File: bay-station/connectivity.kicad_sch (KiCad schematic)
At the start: 4 parts, among them U3 ESP32-S3-WROOM-1

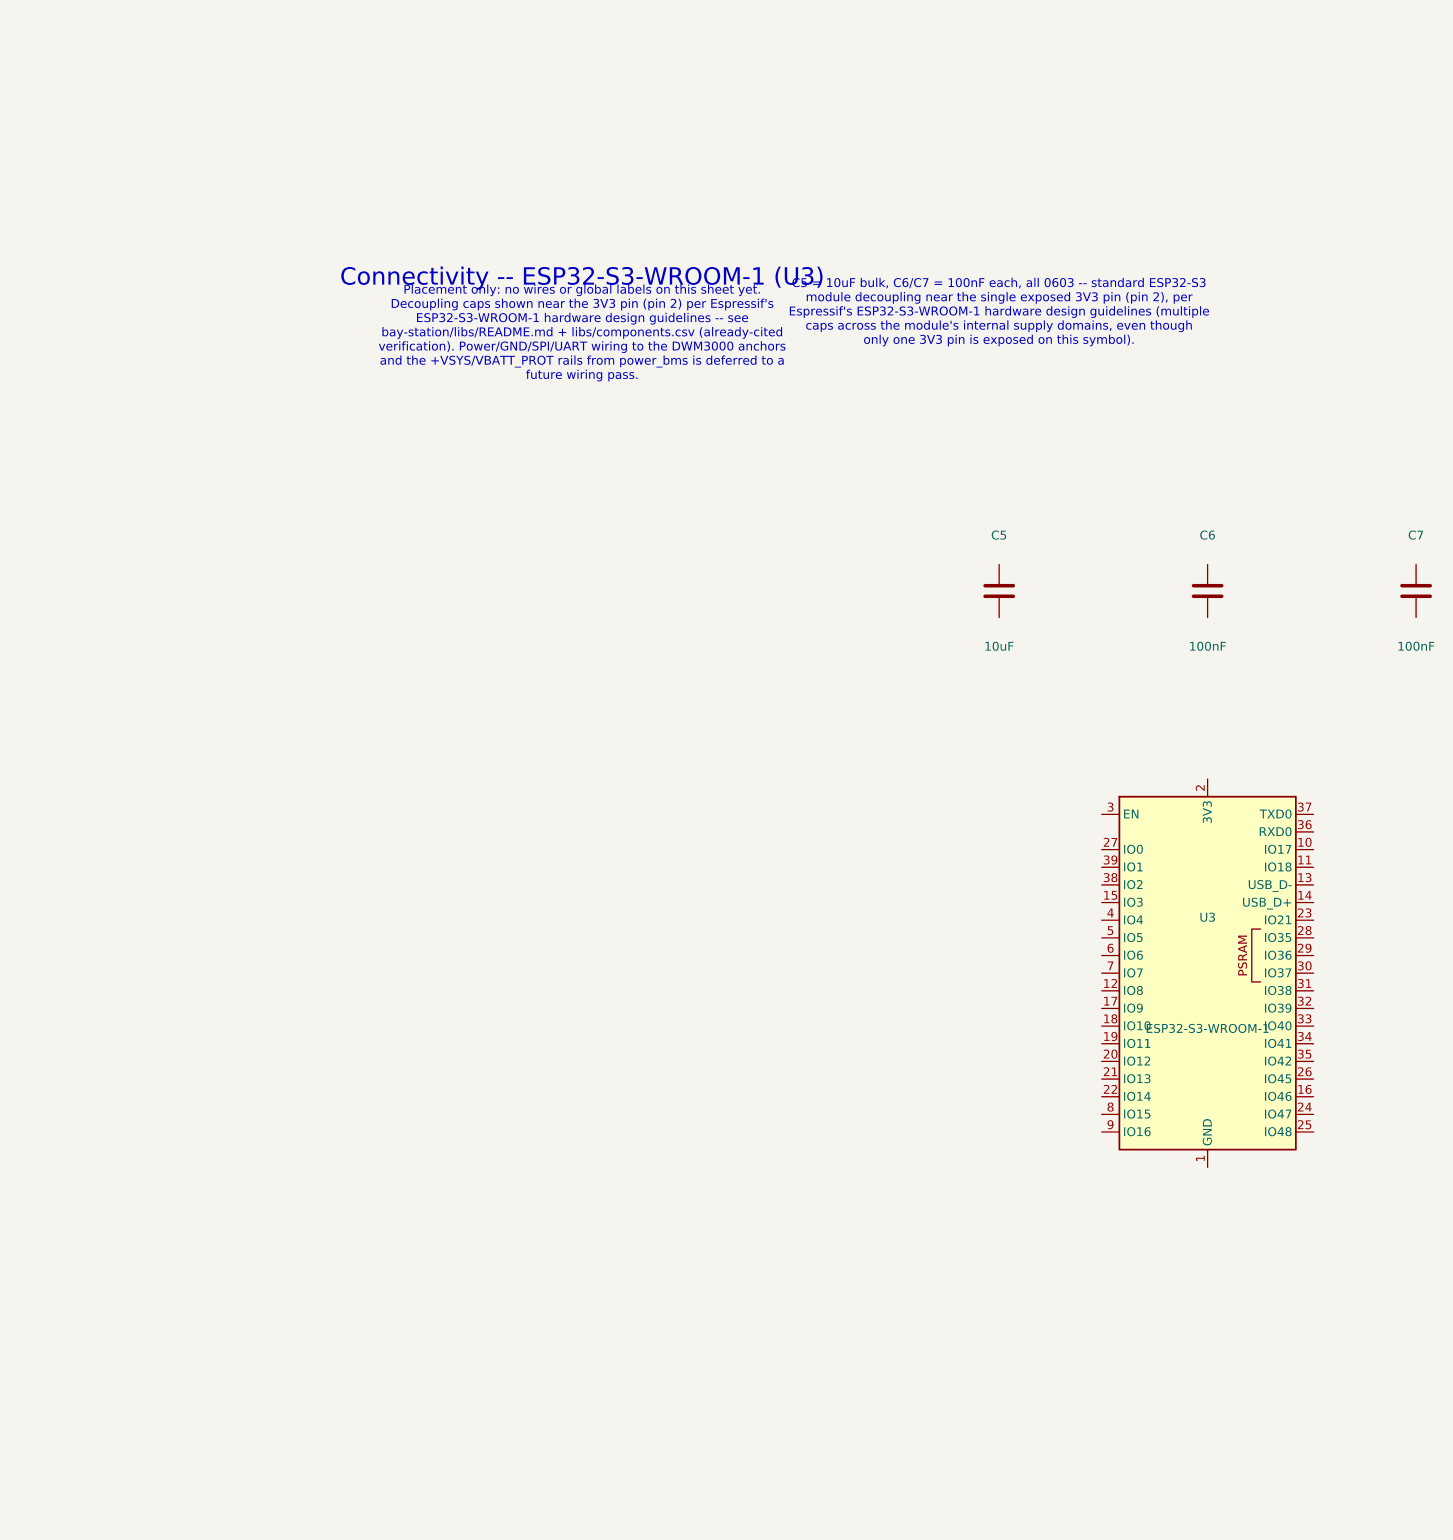
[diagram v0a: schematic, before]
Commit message: Bay station: discrete DW3210 array on a shared clock, Nordic BT840 host
Two coupled changes, both forced by the positioning scheme.

UWB ARRAY. TDoA compares timestamps across receivers, so they must share a
time base. The DWM3000 module makes that impossible -- its 24 pins contain
no clock pin and its crystal is internal and unreachable, so four of them
cannot be synchronised at any price. The bare DW3000 IC can: Datasheet v1.3
Table 10 states a 38.4 MHz signal may be supplied from an external reference
via the XTI overdrive pin. Four DW3210s (QFN40, not the 52-ball WLCSP
DW3110 the module is built on) now sit on one PCB sharing one TCXO through
a 1:4 low-skew buffer, with the antennas remote on ~1-2 m SMA coax. This
makes synchronisation structurally absent rather than solved.

uwb_anchors.kicad_sch renamed to uwb_array.kicad_sch -- the four receivers
are one on-board array, not distributed anchor units. U4 is A0, the CENTER
anchor; U5-U7 are A1-A3 outer. They are not interchangeable peers.

New clock_dist.kicad_sch holds the shared reference network. Placed are only
the passives the datasheet actually specifies: 2200 pF AC coupling into each
XTI and 1 pF from each XTO to ground, both required only because an external
clock is used. TCXO and buffer parts are not yet selected.

HOST MCU. The uplink moved from WiFi-to-internet to BLE-to-a-laptop, and
WiFi was the only thing keeping this board off Nordic. ESP32-S3-WROOM-1 is
replaced by a Fanstel BT840 (nRF52840), which gives one toolchain across
both boards and aligns with Qorvo's DW3000 reference stack -- easing the
multi-instance driver work that sits on the critical path. Note the
ESP32-S3 is BLE-only with no Classic/SPP, so the laptop link is a GATT
service.

programming_debug collapsed accordingly: Nordic programs over SWD, so the
boot straps, EN RC delay, BOOT button and the data-capable USB-C are gone,
replaced by a 2x5 ARM Cortex Debug header. That RESOLVES the long-standing
two-USB-C open item by deletion -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
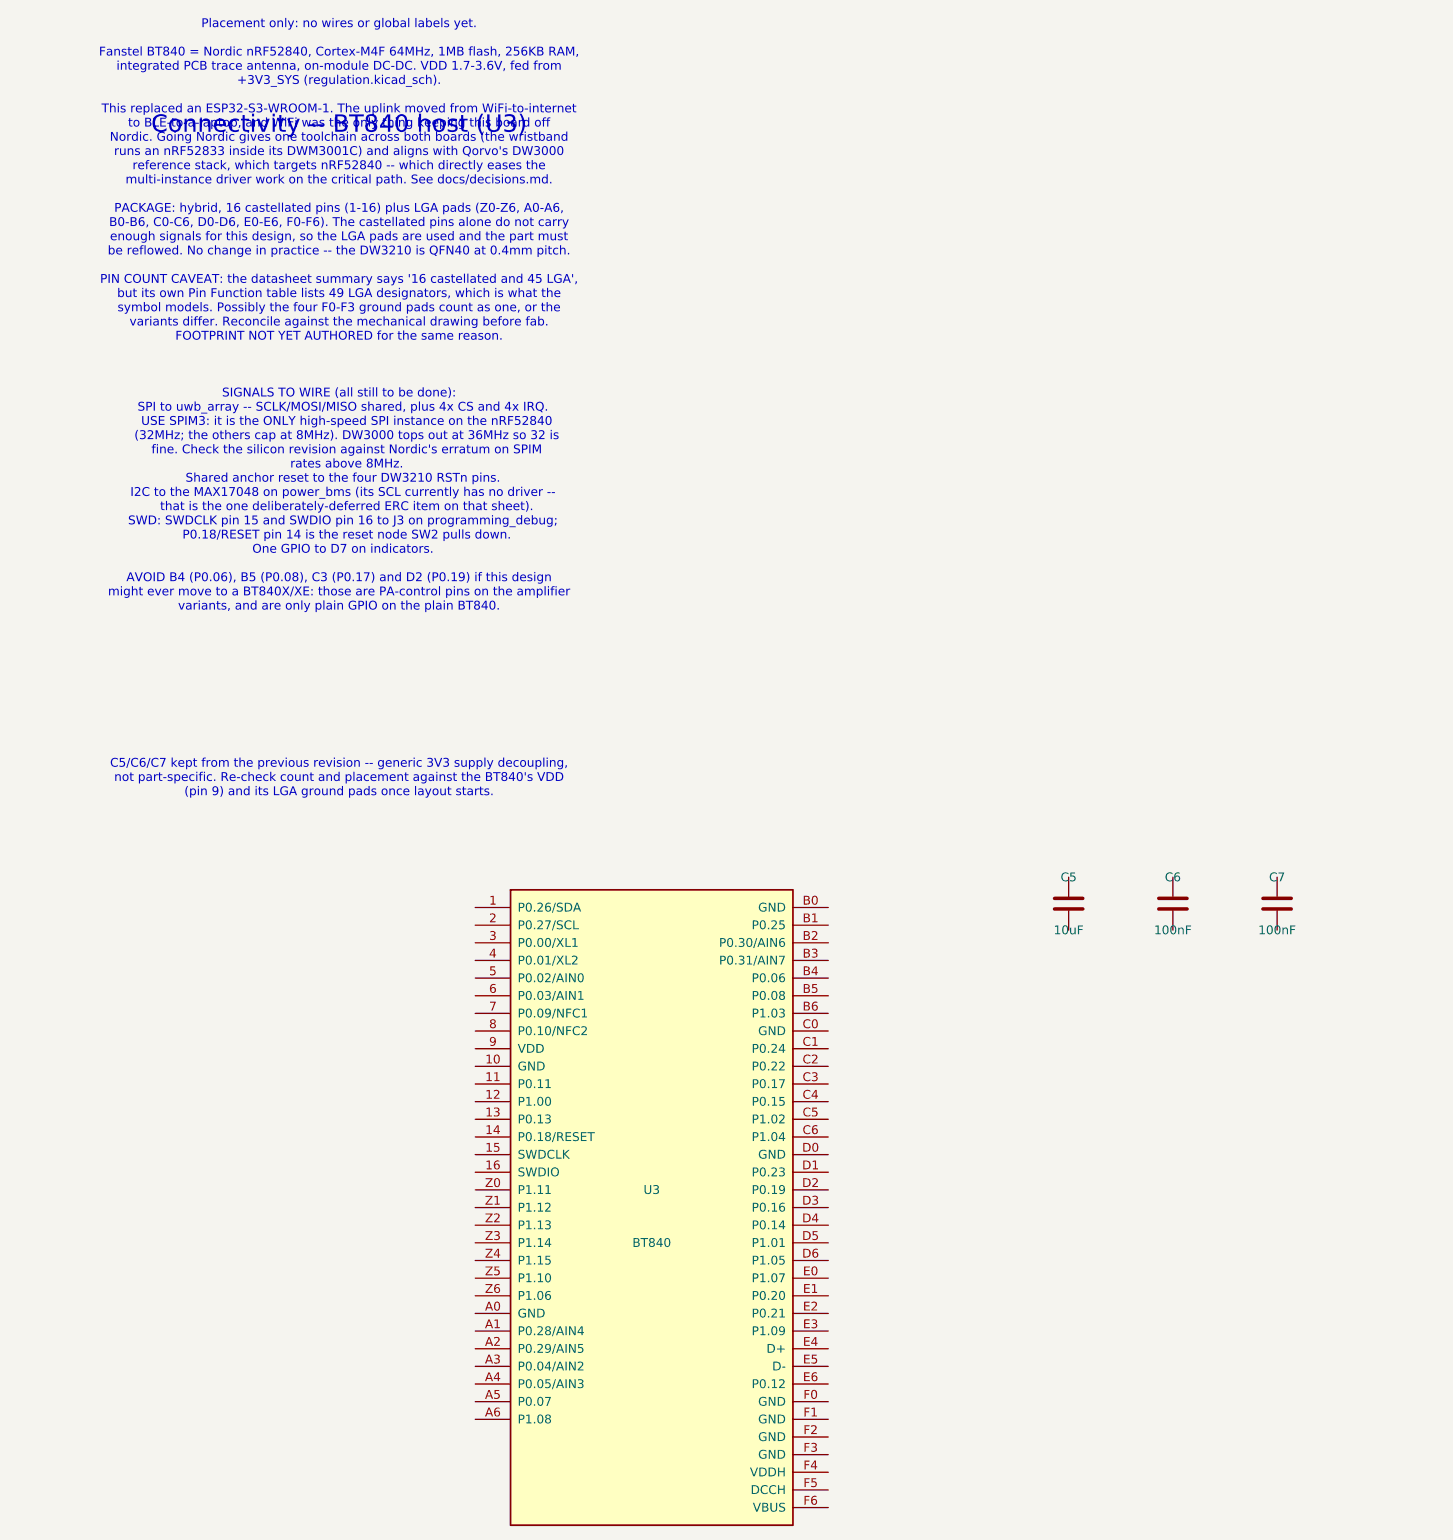
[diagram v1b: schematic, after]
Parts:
- removed U3: ESP32-S3-WROOM-1, RF_Module:ESP32-S3-WROOM-1, symbol RF_Module:ESP32-S3-WROOM-1
- added U3: BT840, symbol bay_station:BT840
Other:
- note added: "C5/C6/C7 kept from the previous revision -- generic 3V3 supply decoupling, not part-specific. Re-check count and placement against the BT840's VDD (pin 9) and its LGA ground pads once layout starts."
- note added: "Connectivity -- BT840 host (U3)"
- note added: "Placement only: no wires or global labels yet. Fanstel BT840 = Nordic nRF52840, Cortex-M4F 64MHz, 1MB flash, 256KB RAM, integrated PCB trace antenna, on-module DC-DC. VDD 1.7-3.6V, fed from +3V3_SYS (regulation.kicad_sch). This replaced an ESP32-S3-WROOM-1. The uplink moved from WiFi-to-internet to BLE-to-a-laptop, and WiFi was the only thing keeping this board off Nordic. Going Nordic gives one 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"
- note added: "SIGNALS TO WIRE (all still to be done): SPI to uwb_array -- SCLK/MOSI/MISO shared, plus 4x CS and 4x IRQ. USE SPIM3: it is the ONLY high-speed SPI instance on the nRF52840 (32MHz; the others cap at 8MHz). DW3000 tops out at 36MHz so 32 is fine. Check the silicon revision against Nordic's erratum on SPIM rates above 8MHz. Shared anchor reset to the four DW3210 RSTn pins. I2C to the MAX17048 on pow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"
- note removed: "C5 = 10uF bulk, C6/C7 = 100nF each, all 0603 -- standard ESP32-S3 module decoupling near the single exposed 3V3 pin (pin 2), per Espressif's ESP32-S3-WROOM-1 hardware design guidelines (multiple caps across the module's internal supply domains, even though only one 3V3 pin is exposed on this symbol)."
- note removed: "Connectivity -- ESP32-S3-WROOM-1 (U3)"
- note removed: "Placement only: no wires or global labels on this sheet yet. Decoupling caps shown near the 3V3 pin (pin 2) per Espressif's ESP32-S3-WROOM-1 hardware design guidelines -- see bay-station/libs/README.md + libs/components.csv (already-cited verification). Power/GND/SPI/UART wiring to the DWM3000 anchors and the +VSYS/VBATT_PROT rails from power_bms is deferred to a future wiring pass."
